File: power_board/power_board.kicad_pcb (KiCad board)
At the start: 4 copper layers, 100 x 100 mm, 111 parts, among them CN1 XT90PW-M.G.Y, CN2 XT60PW-M, Q1 BSC0702LS, Q2 BSC0702LS, Q3 BSC0702LS, Q4 BSC0702LS, Q5 BSC0702LS, Q6 BSC0702LS, U1 STM32L431KCUx, U10 LP2985-33DBVR, U11 LP2985-33DBVR, U12 LP2985-33DBVR, U2 INA180A1, U3 UCC27282DRCR, U4 66565S0M3, U5 UCC27282DRCR, U6 66565S0M3, U7 UCC27282DRCR, U8 66565S0M3, U9 LM5163DDAR

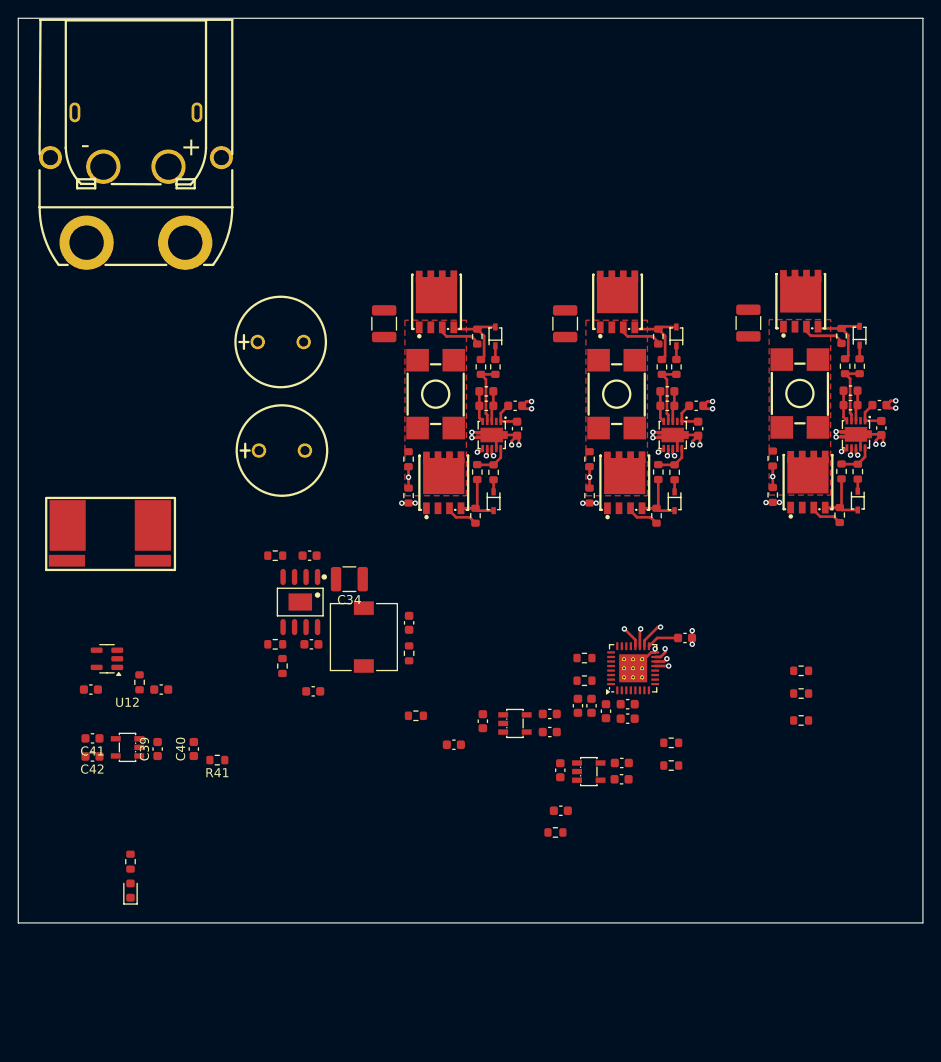
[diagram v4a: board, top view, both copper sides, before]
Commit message: Complete layout, and copper zone design
TODO!!!: move DCDC zone from GND area to PGND(current+)
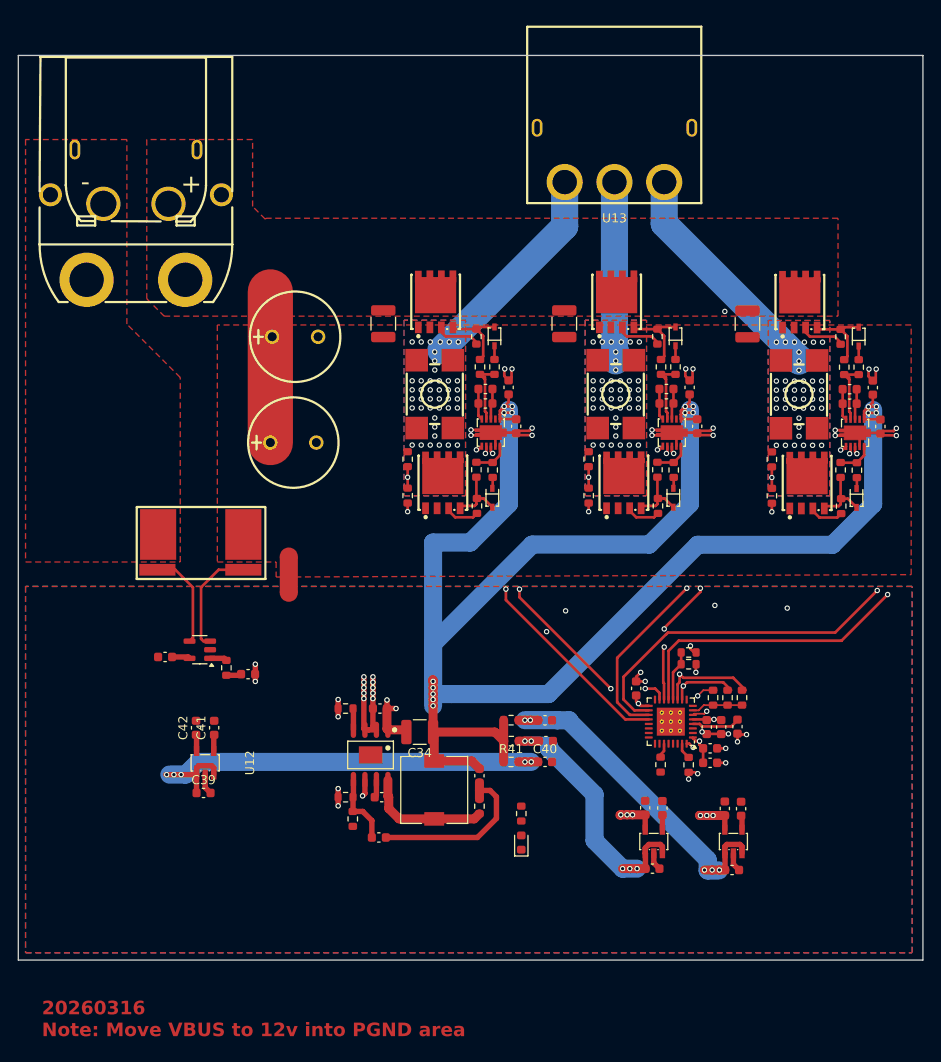
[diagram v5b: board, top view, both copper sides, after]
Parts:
- added NT1: NetTie_2, NetTie:NetTie-2_SMD_Pad2.0mm, F.Cu at (49.9, 80.5)
- added U13: MR60PW-M.G.B, esc-library:CONN-TH_MR60PW, F.Cu at (85.9, 34.1)
- moved D7 43.5 mm to (75.6, 110.1)
- moved R40 43.5 mm to (75.6, 106.9)
- moved C40 38.9 mm to (78.2, 101.2), turned to 0 degrees
- moved R41 32.5 mm to (74.5, 101.2), turned to 0 degrees
- moved C28 24.8 mm to (90.1, 113.0), turned to 0 degrees
- moved C27 22.0 mm to (98.9, 113.2), turned to 0 degrees
- moved U11 20.1 mm to (90.2, 110.0), turned to -90 degrees
- moved C34 18.6 mm to (64.4, 97.9)
- moved R38 18.6 mm to (57.0, 107.5)
- moved C24 18.6 mm to (60.0, 95.3)
- moved C29 18.6 mm to (60.2, 105.1)
- moved R36 18.6 mm to (56.2, 95.3)
- moved R39 18.6 mm to (56.2, 105.1)
- moved U9 18.6 mm to (58.9, 100.4)
- moved C33 18.6 mm to (71.0, 102.7)
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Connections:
- C10 pad 2: GNDPWR -> /curret_sense/current+
- C14 pad 2: GNDPWR -> /curret_sense/current+
- C15 pad 2: GNDPWR -> /curret_sense/current+
- C19 pad 2: GNDPWR -> /curret_sense/current+
- C20 pad 2: GNDPWR -> /curret_sense/current+
- C9 pad 2: GNDPWR -> /curret_sense/current+
- U1 pad 10: /mcu/MOTOR_PHASE_FB_B -> /half_bridge_1/MOTOR_PHASE_FB
- U1 pad 11: /mcu/MOTOR_PHASE_FB_C -> /half_bridge_2/MOTOR_PHASE_FB
- U1 pad 6: /mcu/MOTOR_PHASE_FB_A -> /half_bridge_0/MOTOR_PHASE_FB
- U3 pad 11: GNDPWR -> /curret_sense/current+
- U3 pad 9: GNDPWR -> /curret_sense/current+
- U5 pad 11: GNDPWR -> /curret_sense/current+
- U5 pad 9: GNDPWR -> /curret_sense/current+
- U7 pad 11: GNDPWR -> /curret_sense/current+
- U7 pad 9: GNDPWR -> /curret_sense/current+
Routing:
- net +12V: track 12.8 -> 211.6 mm, vias 3 -> 20
- net VBUS: track 0.00 -> 129.3 mm, vias 0 -> 12
- net Net-(U12-ON/~{OFF}): track 0.00 -> 51.8 mm, vias 0 -> 5
- net /half_bridge_0/MOTOR_PHASE_FB: track 2.38 -> 53.3 mm, vias 1 -> 3
- net /curret_sense/current+: track 11.1 -> 59.3 mm, vias 0 -> 18
- net GNDPWR: track 43.2 -> 0.00 mm, vias 18 -> 0
- net Net-(U10-ON/~{OFF}): track 0.00 -> 39.0 mm, vias 0 -> 5
- net /half_bridge_2/MOTOR_PHASE_FB: track 2.38 -> 40.4 mm, vias 1 -> 2
- net /half_bridge_1/MOTOR_PHASE_FB: track 2.38 -> 40.2 mm, vias 1 -> 2
- net Net-(U11-ON/~{OFF}): track 0.00 -> 30.9 mm, vias 0 -> 5
- net +3V3: track 3.59 -> 34.0 mm, vias 0 -> 5
- net /half_bridge_2/MOTOR_PHASE: track 8.66 -> 34.6 mm, vias 0 -> 42
- net GND: track 9.64 -> 34.6 mm, vias 9 -> 27
- net /half_bridge_0/MOTOR_PHASE: track 8.66 -> 32.9 mm, vias 0 -> 42
- net +3V3A: track 0.00 -> 19.6 mm, vias 0 -> 4
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- added copper zone on F.Cu, net /curret_sense/current+
- added copper zone on B.Cu, net /half_bridge_0/MOTOR_PHASE
- added copper zone on B.Cu, net /half_bridge_1/MOTOR_PHASE
- added copper zone on B.Cu, net /half_bridge_2/MOTOR_PHASE
- added copper zone on B.Cu, net GND
- added copper zone on F.Cu, net GND
- added copper zone on In2.Cu, net GND
- added copper zone on F.Cu, net GNDPWR
- added copper zone on F.Cu, net VBUS
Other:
- board text added: "20260316 Note: Move VBUS to 12v into PGND area"

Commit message: All drc error solved
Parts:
- added C43: 22u, Capacitor_SMD:C_1210_3225Metric, F.Cu at (55.8, 36.2)
- added J1: Conn_ARM_SWD_TagConnect_TC2030-NL, Connector:Tag-Connect_TC2030-IDC-NL_2x03_P1.27mm_Vertical, F.Cu at (82.9, 103.0)
- NT1: footprint NetTie:NetTie-2_SMD_Pad2.0mm -> NetTie:NetTie-2_THT_Pad0.3mm
- U1: footprint Package_DFN_QFN:QFN-32-1EP_5x5mm_P0.5mm_EP3.1x3.1mm_ThermalVias -> Package_DFN_QFN:QFN-32-1EP_5x5mm_P0.5mm_EP3.1x3.1mm
- moved C30 85.6 mm to (65.7, 24.1), turned to 180 degrees
- moved D7 84.6 mm to (49.1, 29.8), turned to -90 degrees
- moved R38 82.1 mm to (68.6, 26.2), turned to -90 degrees
- moved R37 80.2 mm to (54.6, 27.6), turned to 90 degrees
- moved R40 78.5 mm to (49.1, 33.0), turned to 90 degrees
- moved R39 77.6 mm to (69.4, 28.6), turned to 0 degrees
- moved C29 76.7 mm to (65.4, 28.6), turned to 0 degrees
- moved L1 75.2 mm to (59.6, 29.4), turned to -90 degrees
- moved C33 73.6 mm to (54.6, 31.0), turned to -90 degrees
- moved U9 67.6 mm to (66.7, 33.3), turned to 0 degrees
- moved C34 61.7 mm to (61.2, 36.2), turned to 0 degrees
- moved R36 58.4 mm to (69.4, 38.4), turned to 180 degrees
- moved C24 57.2 mm to (65.6, 38.4), turned to 180 degrees
- moved R17 40.8 mm to (97.4, 93.8), turned to 0 degrees
- moved C40 37.4 mm to (41.1, 105.7)
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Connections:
- C24 pad 2: GND -> /curret_sense/current+
- C25 pad 2: GND -> /curret_sense/current+
- C26 pad 2: GND -> /curret_sense/current+
- C34 pad 2: GND -> /curret_sense/current+
- C39 pad 2: GND -> /curret_sense/current+
- CN1 pad 3: GNDPWR -> unconnected-(CN1-Pad3)
- CN1 pad 4: GNDPWR -> unconnected-(CN1-Pad4)
- CN2 pad 3: GNDPWR -> unconnected-(CN2-Pad3)
- CN2 pad 4: GNDPWR -> unconnected-(CN2-Pad4)
- R36 pad 1: GND -> /curret_sense/current+
- R39 pad 2: GND -> /curret_sense/current+
- U13 pad 4: GNDPWR -> unconnected-(U13-Pad4)
- U13 pad 5: GNDPWR -> unconnected-(U13-Pad5)
- U9 pad 1: GND -> /curret_sense/current+
- U9 pad 9: GND -> /curret_sense/current+
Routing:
- net VBUS: track 129.3 -> 26.1 mm, vias 12 -> 0
- net +12V: track 211.6 -> 134.1 mm, vias 20 -> 30
- net /curret_sense/I_OUT: track 1.68 -> 59.9 mm, vias 0 -> 2
- net /mcu/V_SENSE: track 5.58 -> 43.9 mm, vias 0 -> 2
- net Net-(U11-ON/~{OFF}): track 30.9 -> 57.6 mm, vias 5 -> 4
- net Net-(U10-ON/~{OFF}): track 39.0 -> 62.0 mm, vias 5 -> 4
- net /half_bridge_2/MOTOR_PHASE: track 34.6 -> 12.1 mm
- net /half_bridge_0/MOTOR_PHASE: track 32.9 -> 11.2 mm
- net /power_converter/PG: track 1.87 -> 22.2 mm, vias 1 -> 2
- net /curret_sense/current+: track 59.3 -> 70.1 mm, vias 18 -> 93
- net Net-(U12-ON/~{OFF}): track 51.8 -> 41.1 mm, vias 5 -> 4
- net +3V3A0: track 3.80 -> 14.0 mm
- net GND: track 34.6 -> 26.9 mm, vias 27 -> 33
- net /mcu/BEMF_REF: track 6.09 -> 11.4 mm
- net /half_bridge_0/MOTOR_PHASE_FB: track 53.3 -> 56.2 mm
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- added copper zone on F.Cu, net +12V
- added copper zone on In2.Cu, net +12V
- added copper zone on B.Cu, net /curret_sense/current+
- added copper zone on In1.Cu, net /curret_sense/current+
- added copper zone on In2.Cu, net /curret_sense/current+
- added copper zone on B.Cu, net GNDPWR
- added copper zone on In1.Cu, net GNDPWR
- added copper zone on In2.Cu, net GNDPWR
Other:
- board text added: "20260316: TODO: Add SWD interface and PWM input port"
- board text removed: "20260316 Note: Move VBUS to 12v into PGND area"

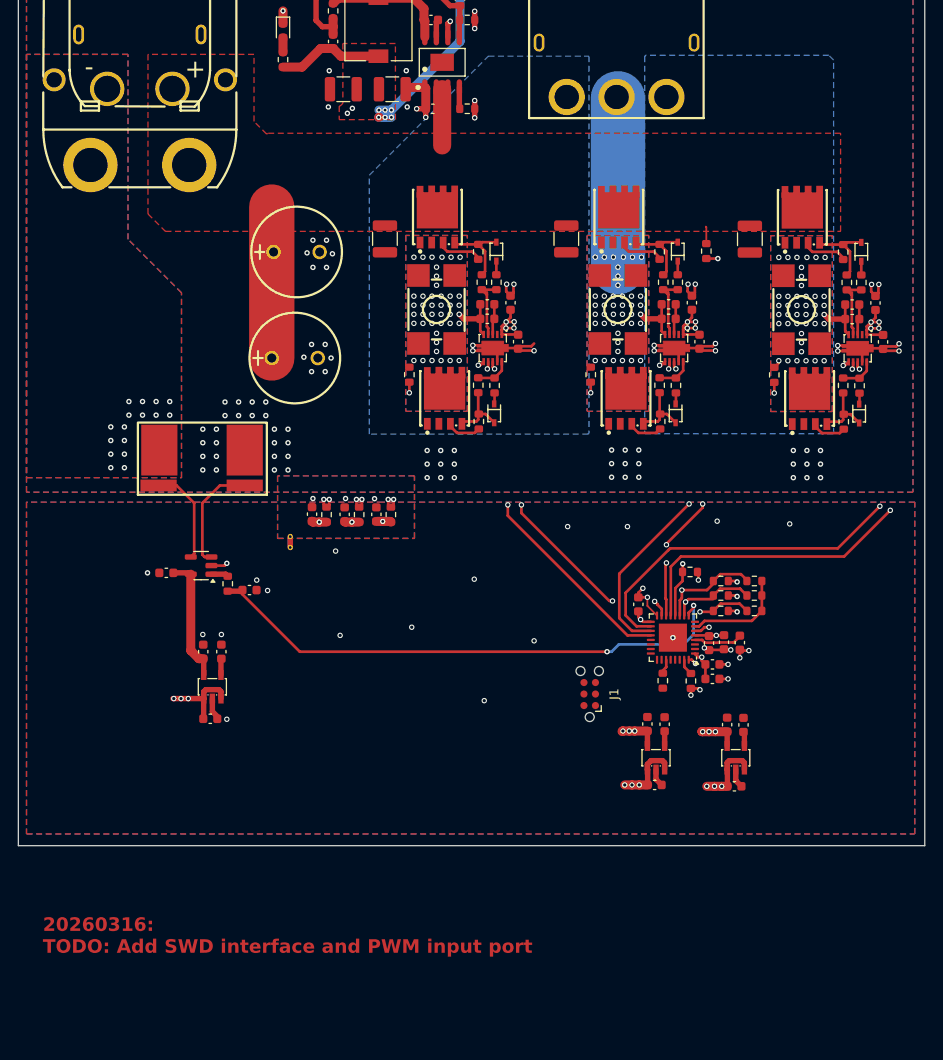
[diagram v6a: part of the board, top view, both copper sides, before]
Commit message: Add testpoint, SWD, and PWM port
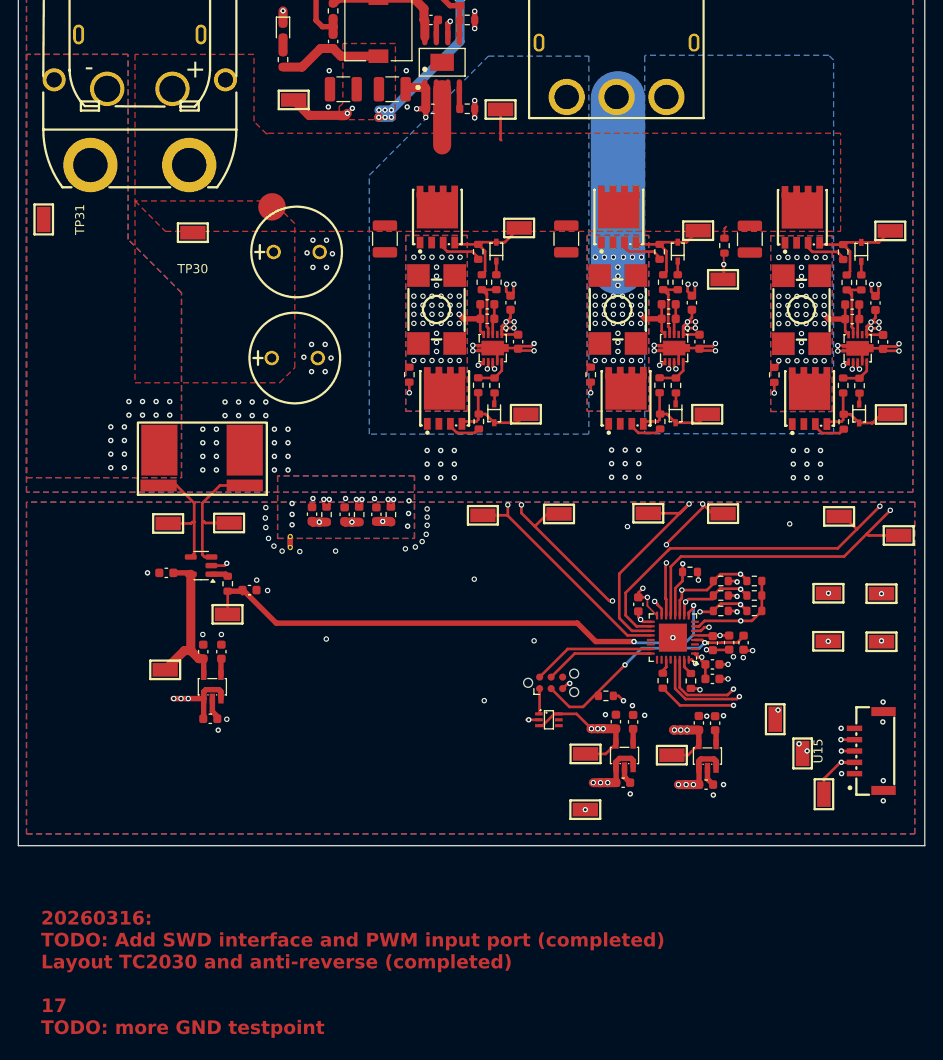
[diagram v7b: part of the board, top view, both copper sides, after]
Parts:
- added R3: 10k, Resistor_SMD:R_0603_1608Metric, F.Cu at (84.7, 103.2)
- added TP1: TestPoint, esc-library:SMD_RH-5015, F.Cu at (106.4, 109.5)
- added TP10: TestPoint, esc-library:SMD_RH-5015, F.Cu at (75.2, 51.5)
- added TP11: TestPoint, esc-library:SMD_RH-5015, F.Cu at (71.2, 83.2)
- added TP12: TestPoint, esc-library:SMD_RH-5015, F.Cu at (79.5, 83.1)
- added TP13: TestPoint, esc-library:SMD_RH-5015, F.Cu at (115.1, 97.2)
- added TP14: TestPoint, esc-library:SMD_RH-5015, F.Cu at (95.9, 72.1)
- added TP15: TestPoint, esc-library:SMD_RH-5015, F.Cu at (94.9, 51.9)
- added TP16: TestPoint, esc-library:SMD_RH-5015, F.Cu at (89.4, 83.0)
- added TP17: TestPoint, esc-library:SMD_RH-5015, F.Cu at (97.7, 83.1)
- added TP18: TestPoint, esc-library:SMD_RH-5015, F.Cu at (115.1, 91.9)
- added TP19: TestPoint, esc-library:SMD_RH-5015, F.Cu at (116.2, 72.1)
- added TP2: TestPoint, esc-library:SMD_RH-5015, F.Cu at (108.8, 114.0)
- added TP20: TestPoint, esc-library:SMD_RH-5015, F.Cu at (116.1, 51.9)
- added TP21: TestPoint, esc-library:SMD_RH-5015, F.Cu at (110.5, 83.4)
- added TP22: TestPoint, esc-library:SMD_RH-5015, F.Cu at (117.0, 85.5)
- added TP23: TestPoint, esc-library:SMD_RH-5015, F.Cu at (109.3, 91.8)
- added TP24: TestPoint, esc-library:SMD_RH-5015, F.Cu at (73.1, 38.5)
- added TP25: TestPoint, esc-library:SMD_RH-5015, F.Cu at (92.0, 109.7)
- added TP26: TestPoint, esc-library:SMD_RH-5015, F.Cu at (82.5, 115.7)
- added TP27: TestPoint, esc-library:SMD_RH-5015, F.Cu at (82.5, 109.6)
- added TP28: TestPoint, esc-library:SMD_RH-5015, F.Cu at (50.3, 37.4)
- added TP29: TestPoint, esc-library:SMD_RH-5015, F.Cu at (36.1, 100.3)
- added TP3: TestPoint, esc-library:SMD_RH-5015, F.Cu at (103.4, 105.8)
- added TP30: TestPoint, esc-library:SMD_RH-5015, F.Cu at (39.1, 52.1)
- added TP31: TestPoint, esc-library:SMD_RH-5015, F.Cu at (22.7, 50.6)
- added TP4: TestPoint, esc-library:SMD_RH-5015, F.Cu at (109.2, 97.2)
- added TP5: TestPoint, esc-library:SMD_RH-5015, F.Cu at (97.6, 57.2)
- added TP6: TestPoint, esc-library:SMD_RH-5015, F.Cu at (43.1, 84.1)
- added TP7: TestPoint, esc-library:SMD_RH-5015, F.Cu at (36.4, 84.2)
- added TP8: TestPoint, esc-library:SMD_RH-5015, F.Cu at (43.0, 94.2)
- added TP9: TestPoint, esc-library:SMD_RH-5015, F.Cu at (75.9, 72.1)
- added U15: SM05B-GHS-TB(LF)(SN), esc-library:CONN-SMD_5P-P1.25_SM05B-GHS-TB-LF-SN, F.Cu at (113.8, 109.3)
- added U2: LM66100DCKR, esc-library:SC-70-6_L2.0-W1.3-P0.65-LS2.1-BL, F.Cu at (78.4, 105.8)
- moved J1 4.43 mm to (78.7, 101.7), turned to 0 degrees
- moved C34 3.48 mm to (87.7, 106.0)
- moved C30 3.48 mm to (86.6, 112.8)
- moved C39 3.48 mm to (85.8, 106.0)
- moved U13 3.48 mm to (86.8, 109.8)
- moved C29 3.13 mm to (95.8, 113.0)
- moved C33 3.13 mm to (96.8, 106.2)
- moved C38 3.13 mm to (95.0, 106.2)
- moved U12 3.13 mm to (95.9, 109.8)
- moved R4 2.09 mm to (97.8, 53.5)
- moved C6 0.57 mm to (98.3, 97.3)
- moved C4 0.41 mm to (96.5, 97.4)
- moved C8 0.41 mm to (99.9, 97.3)
- renumbered C37 to C1, C8 to C10, C9 to C11, C10 to C12, C11 to C13, C12 to C14, C13 to C15, C14 to C16, C15 to C17, C16 to C18, C17 to C19, C38 to C2, C18 to C20, C19 to C21, C20 to C22, C21 to C23, C22 to C24, C23 to C25, C24 to C26, C25 to C27, C26 to C28, C27 to C29, C1 to C3, C28 to C30, C29 to C31, C30 to C32, C31 to C33, C32 to C34, C33 to C35, C43 to C36, C34 to C37, C35 to C38, C36 to C39, C2 to C4, C39 to C40, C40 to C41, C41 to C42, C42 to C43, C3 to C5, C4 to C6, C5 to C7, C6 to C8, C7 to C9, R9 to R10, R10 to R11, R11 to R12, R12 to R13, R13 to R14, R14 to R15, R15 to R16, R16 to R17, R17 to R18, R18 to R19, R19 to R20, R20 to R21, R21 to R22, R22 to R23, R23 to R24, R24 to R25, R25 to R26, R26 to R27, R27 to R28, R28 to R29, R29 to R30, R30 to R31, R31 to R32, R32 to R33, R33 to R34, R34 to R35, R35 to R36, R36 to R37, R37 to R38, R38 to R39, R3 to R4, R39 to R40, R40 to R41, R41 to R42, R4 to R5, R5 to R6, R6 to R7, R7 to R8, R8 to R9, U13 to U1, U8 to U10, U9 to U11, U10 to U12, U11 to U13, U12 to U14, U1 to U3, U2 to U4, U3 to U5, U4 to U6, U5 to U7, U6 to U8, U7 to U9
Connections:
- C8 pad 2: Net-(U1-NRST) -> /mcu/~{RST}
- J1 pad 1: unconnected-(J1-VCC-Pad1) -> Net-(J1-VCC)
- J1 pad 2: unconnected-(J1-SWDIO-Pad2) -> /mcu/SWDIO
- J1 pad 3: unconnected-(J1-~{RESET}-Pad3) -> /mcu/~{RST}
- J1 pad 4: unconnected-(J1-SWCLK-Pad4) -> /mcu/SWDCLK
- J1 pad 5: unconnected-(J1-GND-Pad5) -> GND
- U3 pad 4: Net-(U1-NRST) -> /mcu/~{RST}
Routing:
- net SIGNAL_INPUT: track 0.00 -> 30.4 mm, vias 0 -> 2
- net /mcu/~{RST}: track 0.00 -> 26.5 mm, vias 0 -> 2
- net TELEMETRY: track 0.00 -> 26.1 mm, vias 0 -> 4
- net TELEMETRY_RX: track 0.00 -> 25.4 mm, vias 0 -> 3
- net /half_bridge_0/MOTOR_PHASE_FB: track 56.2 -> 73.4 mm, vias 3 -> 5
- net /half_bridge_1/MOTOR_PHASE_FB: track 40.7 -> 57.5 mm, vias 2 -> 4
- net +3V3: track 34.0 -> 50.2 mm, vias 5 -> 6
- net VBUS: track 26.1 -> 12.3 mm
- net /mcu/SWDIO: track 0.00 -> 13.5 mm
- net /mcu/SWDCLK: track 0.00 -> 12.1 mm
- net /mcu/BEMF_REF: track 11.4 -> 22.4 mm, vias 0 -> 2
- net /half_bridge_2/MOTOR_PHASE_FB: track 39.3 -> 49.9 mm, vias 2 -> 4
- net +12V: track 134.1 -> 140.8 mm
- net Net-(U1-NRST): track 5.37 -> 0.00 mm
- net /half_bridge_1/DRIVER_HIGH: track 36.9 -> 41.8 mm
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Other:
- board text added: "20260316: TODO: Add SWD interface and PWM input port (completed) Layout TC2030 and anti-reverse (completed) 17 TODO: more GND testpoint"
- board text removed: "20260316: TODO: Add SWD interface and PWM input port"

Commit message: Complete all design, pass DRC
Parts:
- added TP32: GND, esc-library:SMD_RH-5015, F.Cu at (36.4, 106.3)
- added TP33: GND, esc-library:SMD_RH-5015, F.Cu at (91.9, 115.7)
- added TP34: GND_P, esc-library:SMD_RH-5015, F.Cu at (49.5, 23.7)
- added TP35: GND, esc-library:SMD_RH-5015, F.Cu at (115.2, 101.5)
- added TP36: GND, esc-library:SMD_RH-5015, F.Cu at (99.5, 116.0)
- added TP37: VSS, esc-library:SMD_RH-5015, F.Cu at (60.6, 72.1)
- added TP38: VSS, esc-library:SMD_RH-5015, F.Cu at (80.6, 72.2)
- added TP39: VSS, esc-library:SMD_RH-5015, F.Cu at (101.1, 72.2)
- added U16: SWD, esc-library:CONN-SMD_5P-P1.25_SM05B-GHS-TB-LF-SN, F.Cu at (70.9, 114.7)
- TP1: value TestPoint -> TELE
- TP10: value TestPoint -> MOS_G_H_0
- TP11, TP16, TP21: value TestPoint -> DRIVE_H
- TP12, TP17, TP22: value TestPoint -> DRIVE_L
- TP13: value TestPoint -> FB_0
- TP14: value TestPoint -> MOS_G_L_1
- TP15: value TestPoint -> MOS_G_H_1
- TP18: value TestPoint -> FB_1
- TP19: value TestPoint -> MOS_G_L_2
- TP2: value TestPoint -> SIG_IN
- TP20: value TestPoint -> MOS_G_H_2
- TP23: value TestPoint -> PHASE_FB_2
- TP24: value TestPoint -> VBUS_IN
- TP25: value TestPoint -> 3V3A
- TP26: value TestPoint -> GND
- TP27: value TestPoint -> 3V3
- TP28: value TestPoint -> 12V
- TP29: value TestPoint -> 3V3A0
- TP3: value TestPoint -> TELE_RX
- TP30: value TestPoint -> VBUS
- TP31: value TestPoint -> GNDPWR
- TP4: value TestPoint -> BEMF_REF
- TP5: value TestPoint -> VBUS_SENSE
- TP6: value TestPoint -> SHUNT_P
- TP7: value TestPoint -> SHUNT_N
- TP8: value TestPoint -> I_SENSE
- TP9: value TestPoint -> MOS_G_L_0
- U15: value SM05B-GHS-TB(LF)(SN) -> CONTROL
- moved U15 1.47 mm to (115.2, 109.2)
- moved TP30 1.27 mm to (38.2, 53.0), turned to -90 degrees
- moved TP31 0.45 mm to (22.4, 50.2)
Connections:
- net Net-(J1-VCC) renamed +3V3SWD
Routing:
- net /mcu/SWDCLK: track 12.1 -> 29.7 mm, vias 0 -> 2
- net /mcu/SWDIO: track 13.5 -> 30.9 mm
- net /mcu/~{RST}: track 26.5 -> 41.4 mm, vias 2 -> 4
- net +3V3SWD: track 2.82 -> 13.2 mm
- net SIGNAL_INPUT: track 30.4 -> 31.8 mm
- net TELEMETRY_RX: track 25.4 -> 26.8 mm
- net TELEMETRY: track 26.1 -> 27.5 mm
- net GND: vias 61 -> 86
- net /curret_sense/current+: vias 100 -> 106
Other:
- board text added: "3-Phase output"
- board text added: "Amplifer"
- board text added: "Buck converter"
- board text added: "Electric Speed Control - Power Board Design By: K.Zhao Fab: 2026 Mar P/N: ESC-POWER-PCBA-0001 HW:v0.1 MECH:v0.1"
- board text added: "GND SWDIO SWDCLK ~{RST} +3V3"
- board text added: "GND TEL_RX TELE SIG_IN GNS"
- board text added: "Half-bridge MOSFET"
- board text added: "MCU"
- board text added: "Power input"
- board text added: "Shunt resistor"
- board text removed: "20260316: TODO: Add SWD interface and PWM input port (completed) Layout TC2030 and anti-reverse (completed) 17 TODO: more GND testpoint"
